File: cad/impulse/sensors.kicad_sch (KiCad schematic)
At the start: 3 parts, among them U3 HP203B

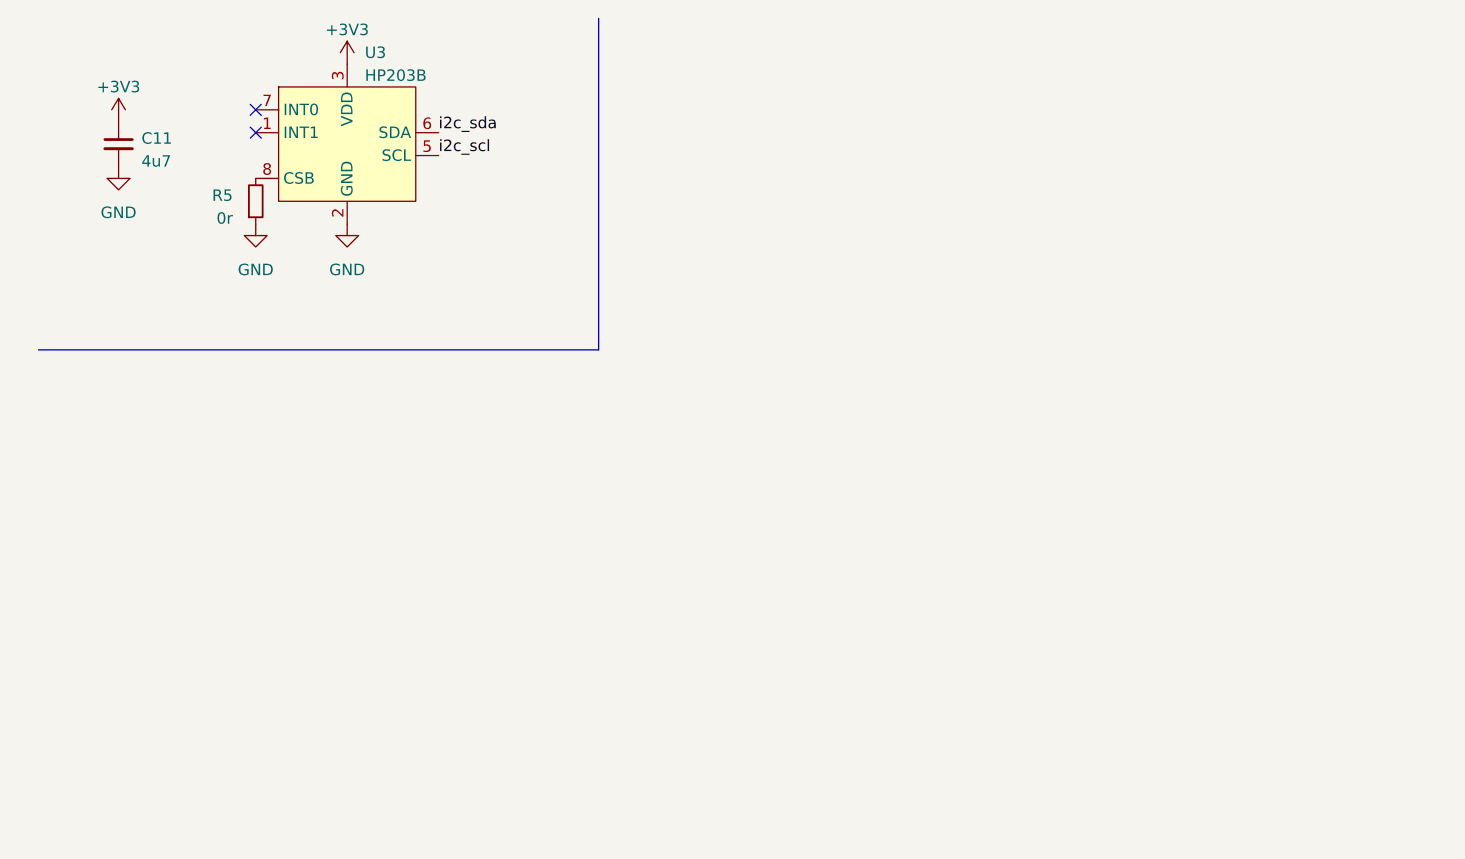
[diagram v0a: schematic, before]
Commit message: Added IMU, button and led. Moved things around.
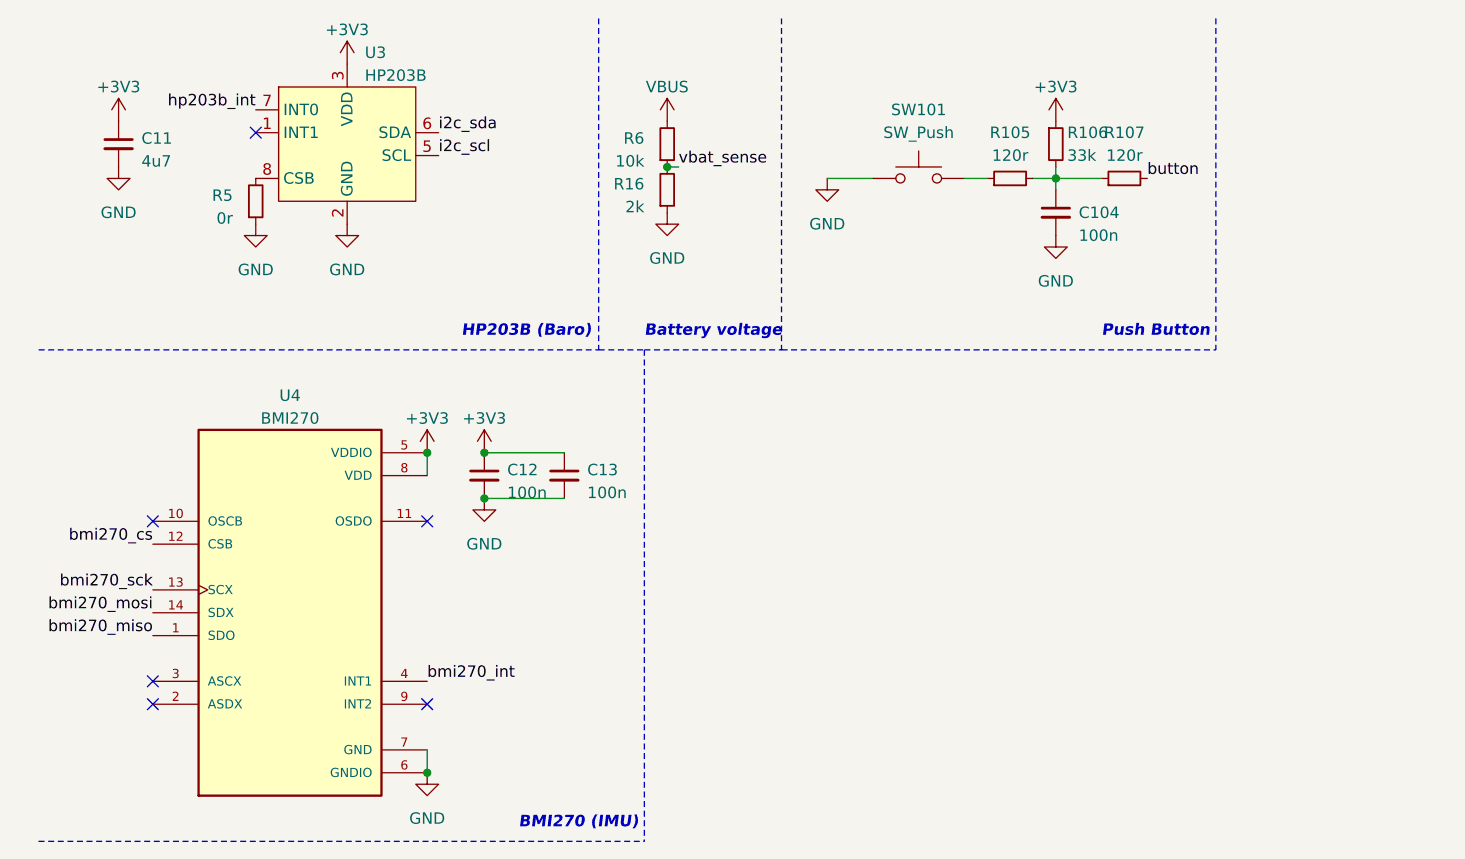
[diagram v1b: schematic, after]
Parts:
- added C104: 100n, Capacitor_SMD:C_0603_1608Metric, symbol Device:C_Small
- added C12, C13: 100n, symbol Device:C_Small
- added R105, R107: 120r, Resistor_SMD:R_0603_1608Metric, symbol Device:R_Small
- added R106: 33k, Resistor_SMD:R_0603_1608Metric, symbol Device:R_Small
- added R16: 2k, symbol Device:R_Small
- added R6: 10k, symbol Device:R_Small
- added SW101: SW_Push, Button_Switch_SMD:SW_SPST_TL3342, symbol Switch:SW_Push
- added U4: BMI270, XDCR_BMI270, symbol BMI270:BMI270
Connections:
- net +3V3: now also C12.1, C13.1, R106.1, U4.5 (VDDIO), U4.8 (VDD)
- net GND: now also C104.2, C12.2, C13.2, R16.1, SW101.1, U4.6 (GNDIO), U4.7 (GND)
- net hp203b_int: now reaches U3.7 (INT0)
- new net: C104.1, R105.2, R106.2, R107.1
- new net: R105.1, SW101.2
- new net VBUS: R6.2
- new net bmi270_cs: U4.12 (CSB)
- new net bmi270_int: U4.4 (INT1)
- new net bmi270_miso: U4.1 (SDO)
- new net bmi270_mosi: U4.14 (SDX)
- new net bmi270_sck: U4.13 (SCX)
- new net button: R107.2
- new net vbat_sense: R16.2, R6.1
- no-connect marks 2 -> 6
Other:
- note added: "BMI270 (IMU)"
- note added: "Battery voltage"
- note added: "HP203B (Baro)"
- note added: "Push Button"

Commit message: Transitioned to global labels when needed.
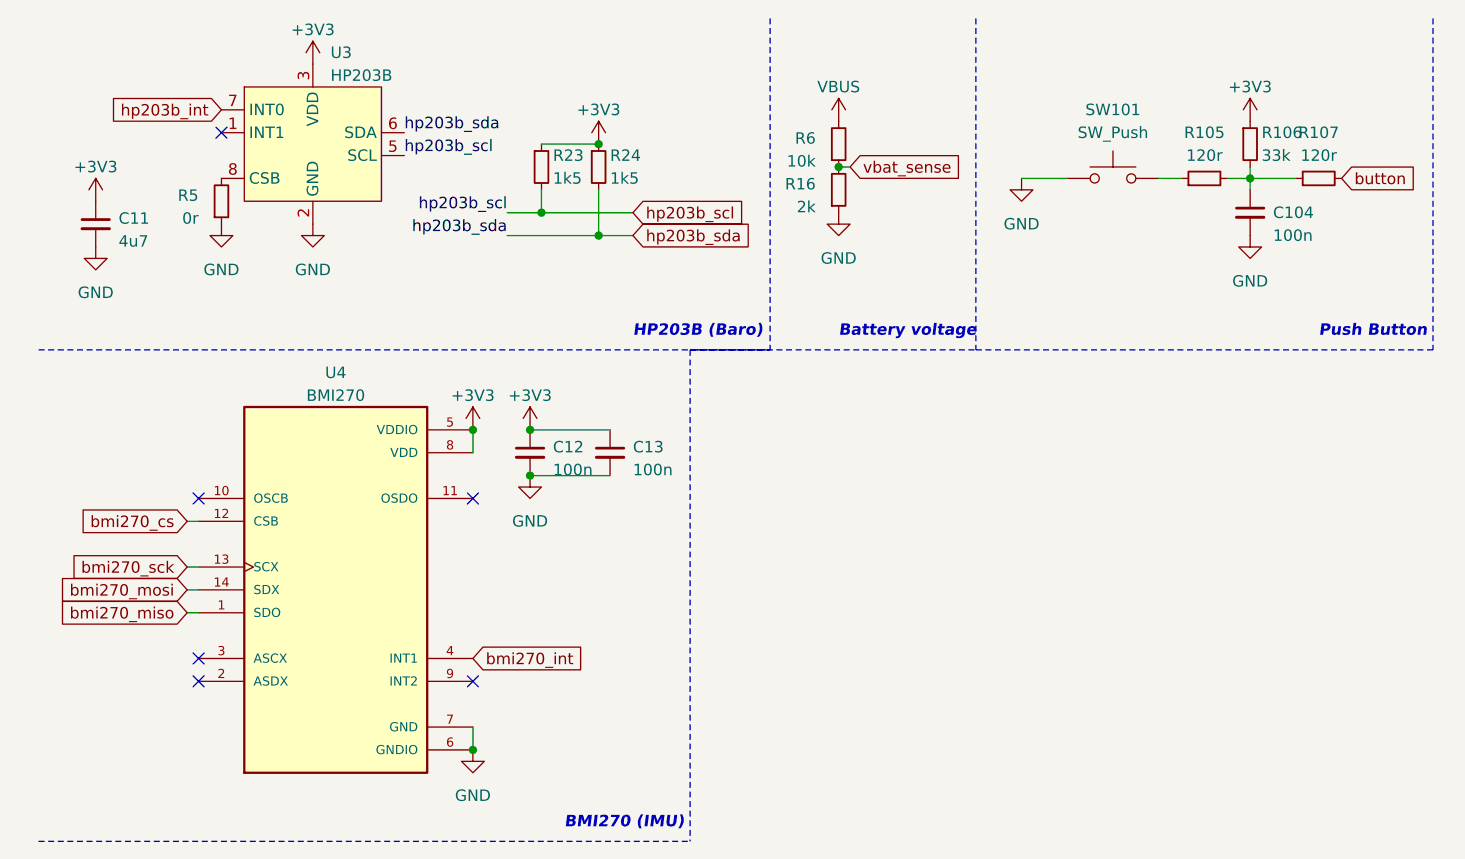
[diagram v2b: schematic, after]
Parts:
- added R23, R24: 1k5, symbol Device:R_Small
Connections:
- net +3V3: now also R23.1, R24.1
- net i2c_scl renamed hp203b_scl
- net hp203b_scl: now also R23.2
- net i2c_sda renamed hp203b_sda
- net hp203b_sda: now also R24.2
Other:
- moved on the sheet: C104, C11, C12, C13, R105, R106, R107, R16, R5, R6, SW101, U3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

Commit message: Finished with LoRa.
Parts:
- renumbered C11 to C12, C12 to C13, C13 to C14, R6 to R16, R23 to R18, R24 to R19, R16 to R22, R5 to R23, U3 to U4, U4 to U5

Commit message: Finnished the design.
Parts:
- added D8: MM3Z3V3, symbol Device:D_Zener_Small
- added R32: 0r, symbol Device:R_Small
- C104: footprint Capacitor_SMD:C_0603_1608Metric -> (none)
- R105, R106, R107: footprint Resistor_SMD:R_0603_1608Metric -> (none)
- SW101: footprint Button_Switch_SMD:SW_SPST_TL3342 -> (none)
- U5: footprint XDCR_BMI270 -> (none)
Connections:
- net bmi270_cs is gone; now on net +3V3: U5.12 (CSB)
- net hp203b_scl is gone; now on net i2c2_scl: R18.2, U4.5 (SCL)
- net hp203b_sda is gone; now on net i2c2_sda: R19.2, U4.6 (SDA)
- net +3V3: now also R32.1
- net GND: now also D8.2 (A)
- net vbat_sense: now also D8.1 (K)
- net bmi270_int: no longer names the net of U5.4 (INT1)
- net bmi270_miso: no longer names the net of U5.1 (SDO)
- net bmi270_miso: now also R32.2
- net bmi270_mosi renamed i2c2_sda
- net bmi270_sck renamed i2c2_scl
- net hp203b_int: no longer names the net of U4.7 (INT0)
- no-connect marks 6 -> 8
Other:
- note added: "I2C addr: 0x69"
- note added: "I2C addr: 0x77"
- note added: "I2C2"
- company: (none) -> markbel
- title: (none) -> Sensors

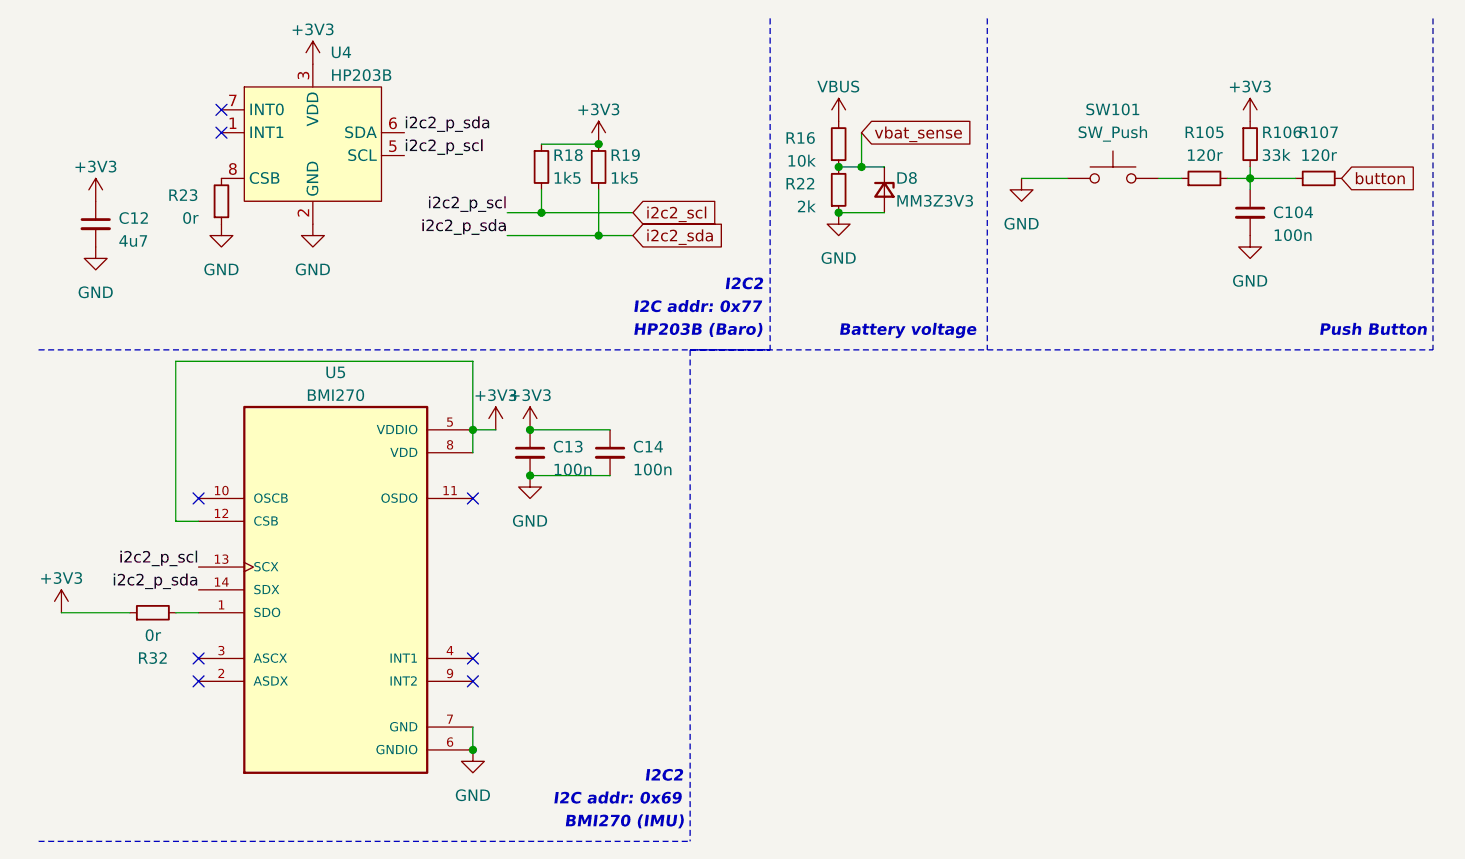
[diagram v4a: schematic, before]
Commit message: Started working on BOM, did consolidation.
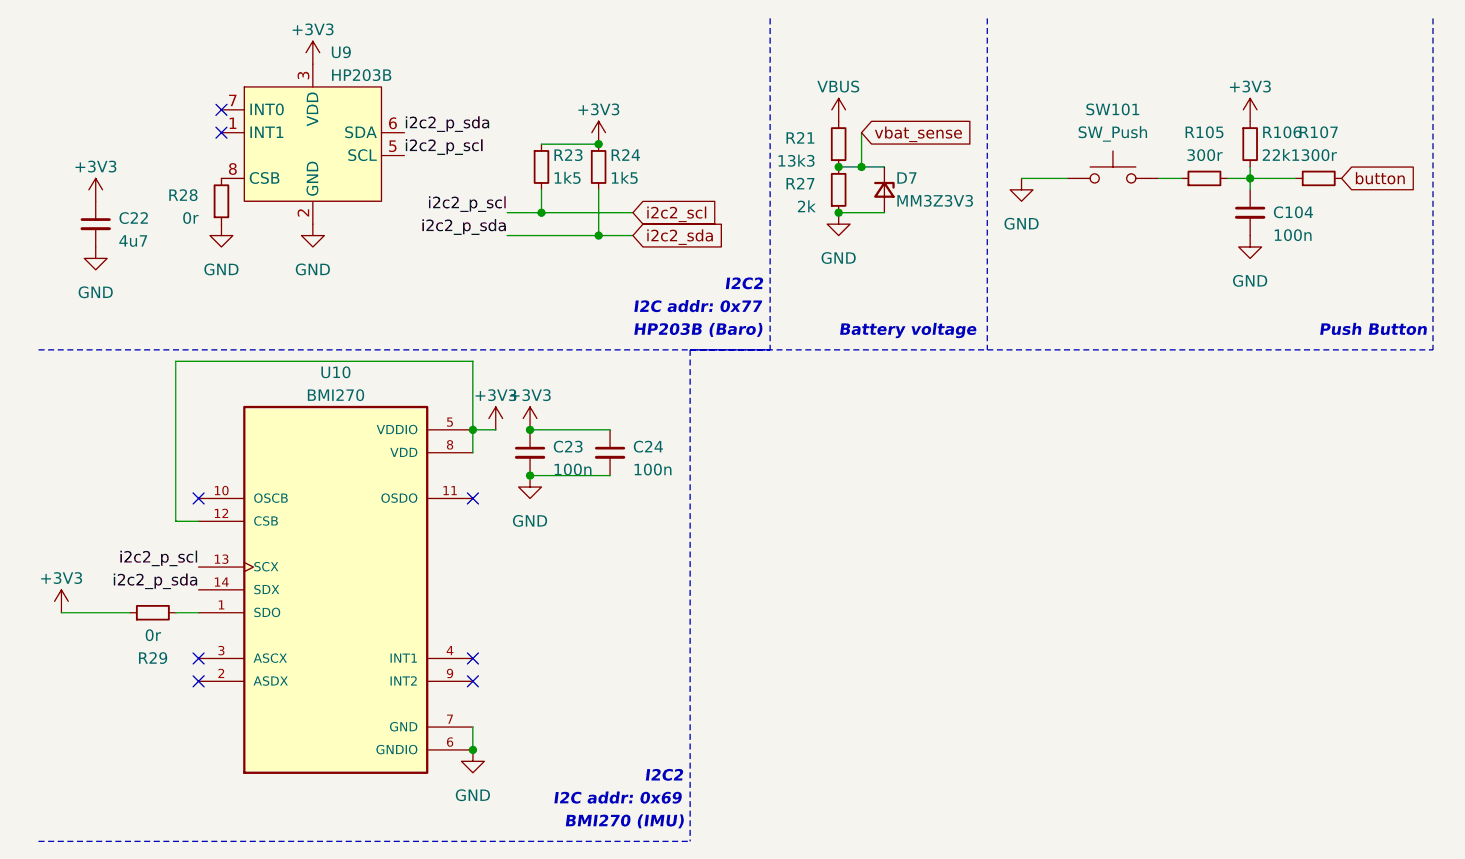
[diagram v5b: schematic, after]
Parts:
- C104: lcsc (none) -> C1525
- C22: renamed from C12; lcsc (none) -> C5360855
- C23: renamed from C13; lcsc (none) -> C1525
- C24: renamed from C14; lcsc (none) -> C1525
- D7: renamed from D8; lcsc (none) -> C2978809
- R105, R107: value 120r -> 300r; lcsc (none) -> C3017471
- R106: value 33k -> 22k1; lcsc (none) -> C5356129
- R21: renamed from R16; value 10k -> 13k3; lcsc (none) -> C3015832
- R23: renamed from R18; lcsc (none) -> C3017483
- R24: renamed from R19; lcsc (none) -> C3017483
- R27: renamed from R22; lcsc (none) -> C3152076
- R28: renamed from R23; lcsc (none) -> C21376
- R29: renamed from R32; lcsc (none) -> C21376
- U10: renamed from U5; lcsc (none) -> C2836813
- U9: renamed from U4; lcsc (none) -> C138665

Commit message: Finished with schematic, starting to route traces.
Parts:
- C104, C23, C24: footprint (none) -> Capacitor_SMD:C_0402_1005Metric
- C22: footprint (none) -> Capacitor_SMD:C_0603_1608Metric
- D7: footprint (none) -> Diode_SMD:D_SOD-323
- R105, R106, R107, R21, R23, R24, R27, R28, R29: footprint (none) -> Resistor_SMD:R_0402_1005Metric
- SW101: footprint (none) -> Button_Switch_SMD:GT-TC029B-H025-L1N; lcsc (none) -> C843669
- U10: footprint (none) -> Package_LGA:LGA-14_3x2.5mm_P0.5mm_LayoutBorder3x4y
- U9: footprint (none) -> Package_DFN_QFN:QFN-8-P09
